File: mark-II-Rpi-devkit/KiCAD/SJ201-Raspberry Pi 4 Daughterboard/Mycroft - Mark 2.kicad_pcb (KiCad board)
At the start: 4 copper layers, 72 x 93 mm, 197 parts, among them J1 Barrel_Jack, J10 Debug Connector, J11 I2S, J12 SCL, J13 USB-PinHeader, J14 SDA, J2 PVDD Jumper, J3 SPKLEFT, J4 SPKRIGHT, J5 PowerTP, J6 Raspberry_Pi_4, J7 USB_B_Micro, J8 MIC, J9 AudioJack3_Ground_Switch, P1 LED, P2 LED, P3 LED, P4 LED, Q3 AO3401A, Q4 2N7002, SW1 MuteMic, U1 XL4501E1, U10 SPK0838HT4H-1, U11 SPK0838HT4H-1, U12 NCP303LSN09, U13 UDA1334ATS, U14 ATtiny402-SS, U2 NCP303LSN09, U3 MAX9744, U4 AMS1117-3.3, U5 SN74LVC125APWR, U6 FE1.1s, U7 MP2359, U8 XMOS-XVF3510, U9 AT25SF161 16MBIT, X1 SG-210STF 24M, Y2 12MHz

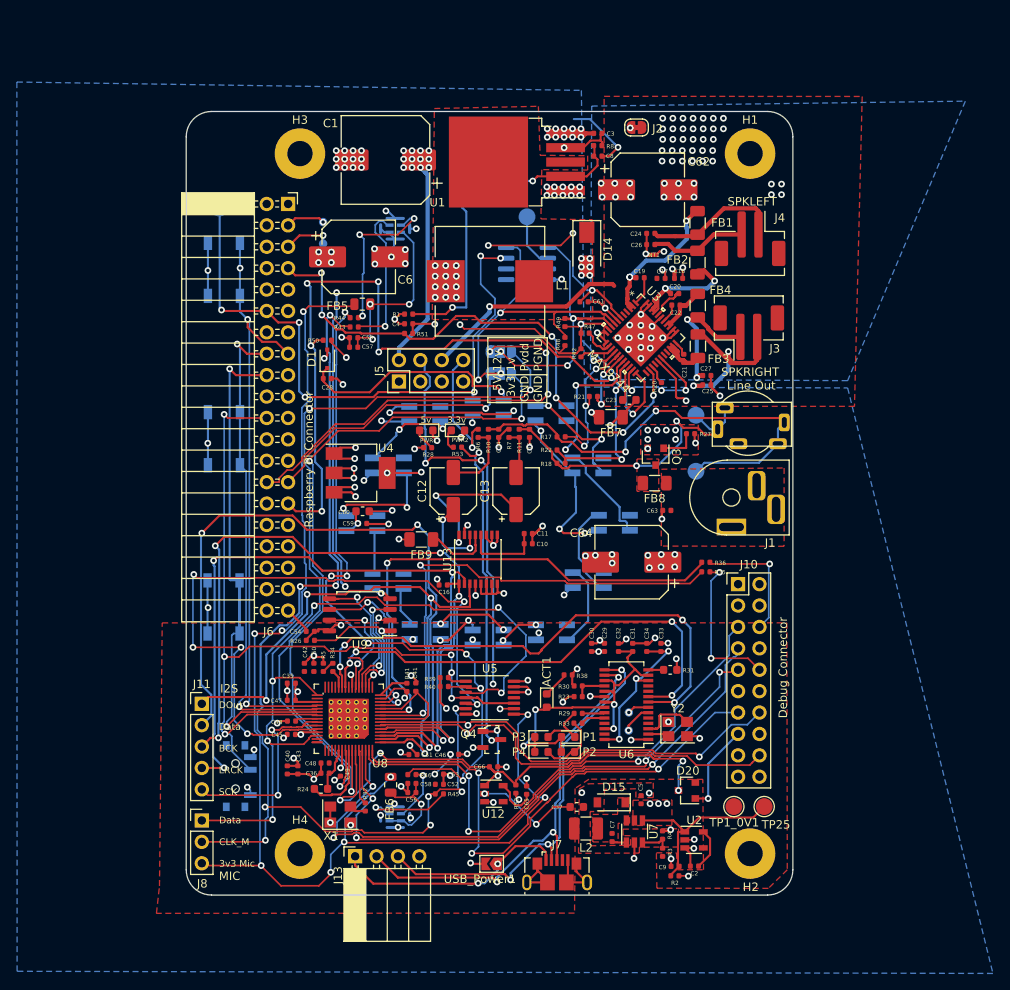
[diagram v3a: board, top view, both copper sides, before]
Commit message: SJ-201 v3, sent to PCB Fab. Removed USB Hub, add in I2S to Line Out
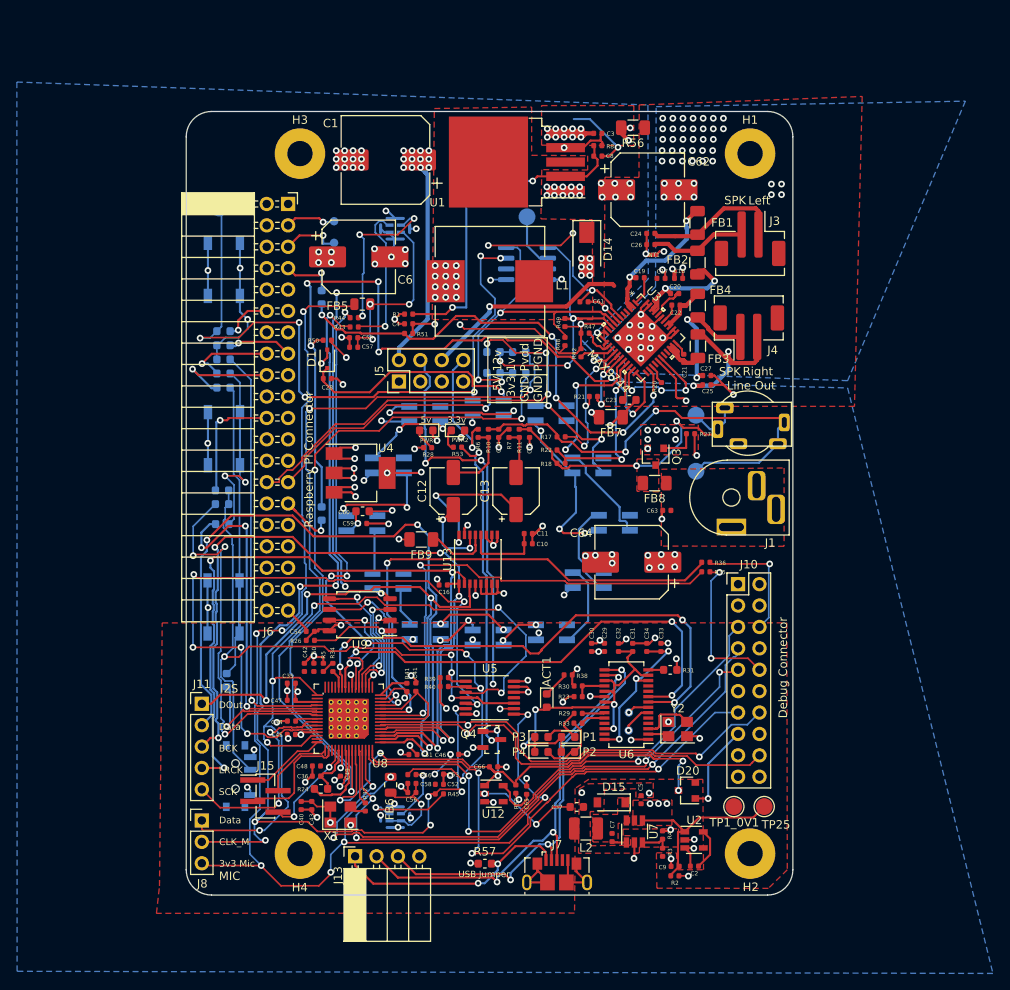
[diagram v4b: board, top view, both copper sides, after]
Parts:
- removed J12: SCL, Jumper:SolderJumper-3_P1.3mm_Bridged2Bar12_RoundedPad1.0x1.5mm_NumberLabels
- removed J14: SDA, Jumper:SolderJumper-3_P1.3mm_Bridged2Bar12_RoundedPad1.0x1.5mm_NumberLabels
- removed J2: PVDD Jumper, Jumper:SolderJumper-2_P1.3mm_Bridged_RoundedPad1.0x1.5mm
- removed USB_Power1: USB Jumper, Jumper:SolderJumper-2_P1.3mm_Open_TrianglePad1.0x1.5mm
- added J15: Output, Connector_PinHeader_1.27mm:PinHeader_1x04_P1.27mm_Vertical_SMD_Pin1Left, F.Cu at (9.40, 81.2)
- added R12: 0R, Resistor_SMD:R_0603_1608Metric, B.Cu at (4.42, 27.8)
- added R13: 0R, Resistor_SMD:R_0603_1608Metric, B.Cu at (4.42, 31.1)
- added R14: 0R, Resistor_SMD:R_0603_1608Metric, B.Cu at (4.42, 32.8)
- added R15: 0R, Resistor_SMD:R_0603_1608Metric, B.Cu at (4.25, 45.0)
- added R16: 0R, Resistor_SMD:R_0603_1608Metric, B.Cu at (16.1, 22.1)
- added R19: 0R, Resistor_SMD:R_0603_1608Metric, B.Cu at (16.1, 47.7)
- added R25: 0R - DNP, Resistor_SMD:R_0603_1608Metric, B.Cu at (39.5, 31.0)
- added R37: 0R - DNP, Resistor_SMD:R_0603_1608Metric, B.Cu at (39.5, 28.6)
- added R54: 0R, Resistor_SMD:R_0603_1608Metric, B.Cu at (36.5, 31.0)
- added R55: 0R, Resistor_SMD:R_0603_1608Metric, B.Cu at (36.5, 28.6)
- added R56: 0R, Resistor_SMD:R_1206_3216Metric, F.Cu at (53.0, 1.93)
- added R57: 0R - DNP, Resistor_SMD:R_0603_1608Metric, F.Cu at (35.5, 89.3)
- added R58: 0R DNP, Resistor_SMD:R_0603_1608Metric, B.Cu at (4.42, 29.4)
- added R59: 0R DNP, Resistor_SMD:R_0603_1608Metric, B.Cu at (4.28, 49.0)
- added R60: 0R DNP, Resistor_SMD:R_0603_1608Metric, B.Cu at (4.80, 67.5)
- added R61: 0R DNP, Resistor_SMD:R_0603_1608Metric, B.Cu at (4.25, 46.6)
- added R9: 0R, Resistor_SMD:R_0603_1608Metric, B.Cu at (4.42, 26.1)
- J3: value SPKLEFT -> SPK
- J4: value SPKRIGHT -> SPK
- S1: value Action -> Button
- S2: value VolUp -> Button
- S3: value VolDown -> Button
- U10, U11: value SPK0838HT4H-1 -> SPK0641HT4H-1
- U4: value AMS1117-3.3 -> NCP565
- moved C40 4.54 mm to (13.7, 82.4)
- moved C43 4.54 mm to (14.9, 82.4)
- moved TP2 1.30 mm to (17.5, 13.0)
- moved TP3 1.30 mm to (17.5, 15.6)
- moved C36 1.08 mm to (15.5, 78.9)
- moved C48 1.08 mm to (15.5, 77.7)
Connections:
- net USB_MICRO_D+ renamed USB_CORAL_D+
- net USB_MICRO_D- renamed USB_CORAL_D-
- C23 pad 2: PGND -> GNDA
- FB7 pad 1: PGND -> GNDA
- J6 pad 12: GPIO18 -> Net-(J6-Pad12)
- J6 pad 15: GPIO22 -> Net-(J6-Pad15)
- J6 pad 16: GPIO23 -> Net-(J6-Pad16)
- J6 pad 18: GPIO24 -> Net-(J6-Pad18)
- J6 pad 22: GPIO25 -> Net-(J6-Pad22)
- J6 pad 29: GPIO5 -> Net-(J6-Pad29)
- J6 pad 7: GPIO4 -> Net-(J6-Pad7)
- U14 pad 1: +5V -> +3V3
- U8 pad 34: GPIO22 -> Net-(R58-Pad2)
- U8 pad 35: GPIO23 -> Net-(R59-Pad2)
- U8 pad 36: GPIO24 -> Net-(R60-Pad2)
- U8 pad 37: GPIO25 -> Net-(R61-Pad2)
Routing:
- net GPIO22: track 71.4 -> 17.1 mm, vias 3 -> 2
- net Net-(R58-Pad2): track 0.00 -> 49.6 mm, vias 0 -> 1
- net Net-(R61-Pad2): track 0.00 -> 46.7 mm, vias 0 -> 3
- net Net-(R59-Pad2): track 0.00 -> 40.2 mm, vias 0 -> 3
- net GPIO23: track 57.2 -> 22.7 mm
- net GPIO24: track 68.2 -> 41.7 mm, vias 2 -> 0
- net GPIO25: track 106.3 -> 81.5 mm, vias 6 -> 4
- net Net-(R60-Pad2): track 0.00 -> 16.7 mm, vias 0 -> 1
- net Net-(J6-Pad22): track 0.00 -> 14.4 mm, vias 0 -> 1
- net TP3: track 0.00 -> 14.1 mm
- net Net-(J6-Pad18): track 0.00 -> 13.0 mm, vias 0 -> 1
- net TP4: track 0.00 -> 12.0 mm, vias 0 -> 2
- net Net-(J6-Pad16): track 0.00 -> 10.4 mm, vias 0 -> 1
- net TP1: track 0.00 -> 9.50 mm
- net TP2: track 0.00 -> 8.63 mm
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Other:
- board text added: "GP02 GP03 GP04 GND GP22 GND SDA GP05 GND"
- board text added: "Left"
- board text added: "Mycroft MK2 v0.67c SJ201-01-03"
- board text added: "Raspi I2C XMOS ----- I2C Selector"
- board text added: "Right"
- board text added: "USB Jumper"
- board text removed: "I2C Selector XMOS I2C Raspi"
- board text removed: "JLCJLCJLCJLC"
- board text removed: "Mycroft MK2 v0.67 SJ201-01-03"
- board text removed: "SDA SCL GP04 GND GP22 GND GP05 GND"
